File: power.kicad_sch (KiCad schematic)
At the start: 4 parts

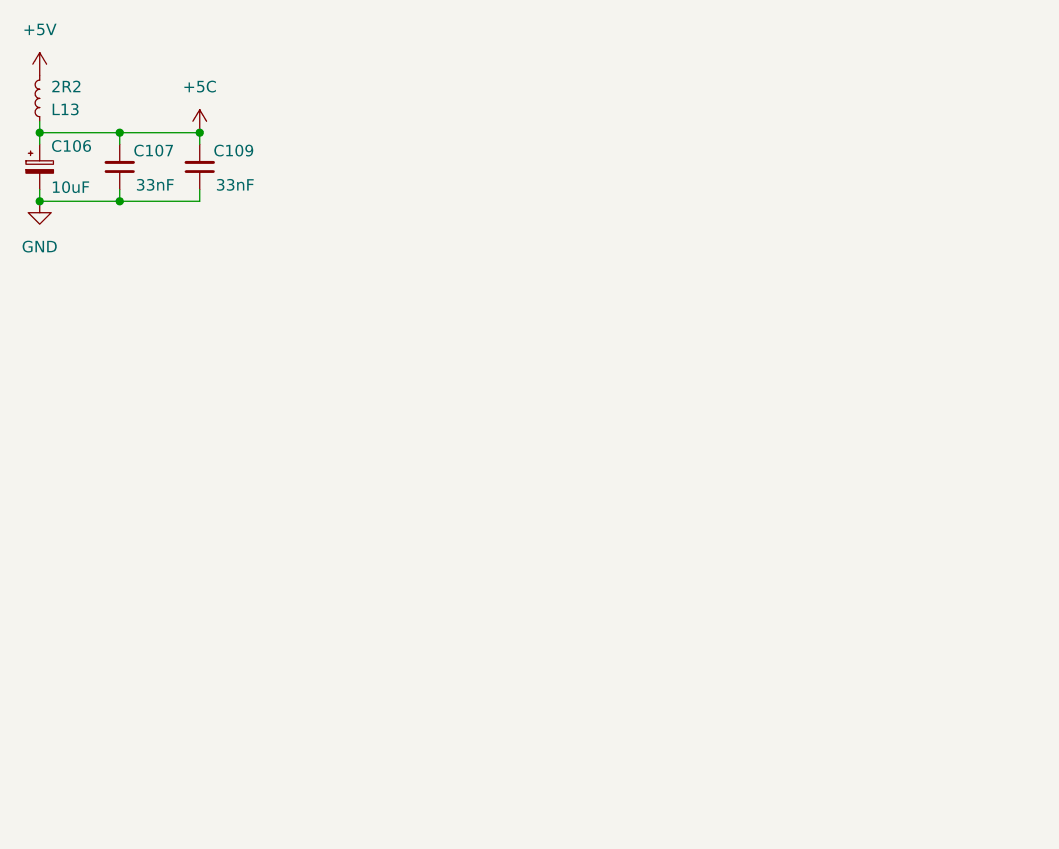
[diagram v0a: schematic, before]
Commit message: add cheeky mean well power swap
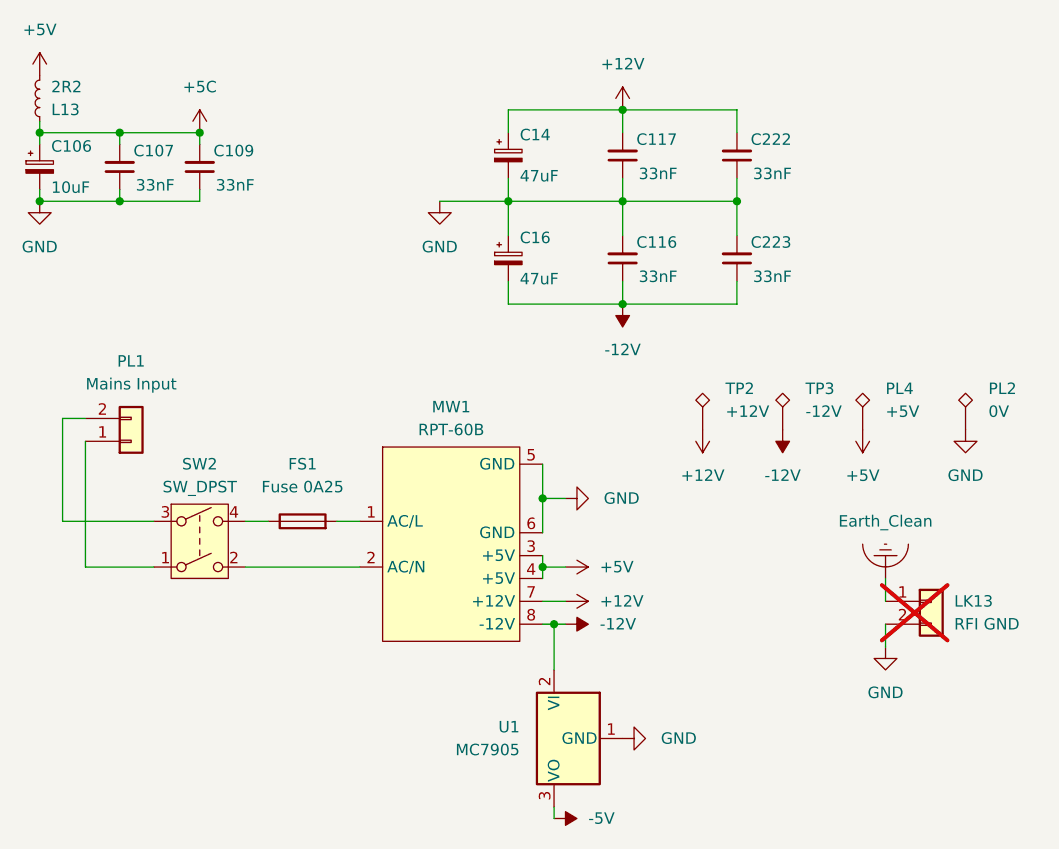
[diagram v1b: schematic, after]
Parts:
- added C116, C117, C222, C223: 33nF, Capacitor_SMD:C_0805_2012Metric, symbol Device:C_Small
- added C14, C16: 47uF, Capacitor_THT:CP_Radial_D8.0mm_P5.00mm, symbol Device:C_Polarized_Small
- added FS1: Fuse 0A25, Fuse:Fuseholder_Clip-5x20mm_Bel_FC-203-22_Lateral_P17.80x5.00mm_D1.17mm_Horizontal, symbol Device:Fuse
- added LK13: RFI GND, Connector_PinHeader_2.54mm:PinHeader_1x02_P2.54mm_Vertical, symbol Connector_Generic:Conn_01x02
- added MW1: RPT-60B, Acorn:RPT-60, symbol Acorn:RPT-60B
- added PL1: Mains Input, Connector_Molex:Molex_KK-396_A-41792-0002_1x02_P3.96mm_Horizontal, symbol Connector_Generic:Conn_01x02
- added PL2: 0V, Acorn:Molex_19708-4003, symbol Connector:TestPoint_Alt
- added PL4: +5V, Acorn:Molex_19708-4003, symbol Connector:TestPoint_Alt
- added SW2: SW_DPST, Button_Switch_THT:SW_Push_2P1T_Toggle_CK_PVA1xxH1xxxxxxV2, symbol Switch:SW_DPST
- added TP2: +12V, Acorn:Molex_19708-4003, symbol Connector:TestPoint_Alt
- added TP3: -12V, Acorn:Molex_19708-4003, symbol Connector:TestPoint_Alt
- added U1: MC7905, Package_TO_SOT_THT:TO-220-3_Horizontal_TabDown, symbol Regulator_Linear:MC7905
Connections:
- net +5V: now also MW1.3 (+5V), MW1.4 (+5V), PL4.1
- net GND: now also C116.2, C117.1, C14.2, C16.1, C222.1, C223.2, LK13.2 (Pin_2), MW1.5 (GND), MW1.6 (GND), PL2.1, U1.1 (GND)
- new net: FS1.1, SW2.4
- new net: FS1.2, MW1.1 (AC/L)
- new net: MW1.2 (AC/N), SW2.2
- new net: PL1.1 (Pin_1), SW2.1
- new net: PL1.2 (Pin_2), SW2.3
- new net +12V: C117.2, C14.1, C222.2, MW1.7 (+12V), TP2.1
- new net -12V: C116.1, C16.2, C223.1, MW1.8 (-12V), TP3.1, U1.2 (VI)
- new net -5V: U1.3 (VO)
- new net Earth_Clean: LK13.1 (Pin_1)

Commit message: fix port reference locations and lock components
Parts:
- C106: footprint Capacitor_THT:CP_Radial_D8.0mm_P5.00mm -> Capacitor_THT:CP_Radial_Tantal_D9.0mm_P5.00mm
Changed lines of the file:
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@@
 			)
 		)
-		(property "Footprint" "Capacitor_THT:CP_Radial_D8.0mm_P5.00mm"
+		(property "Footprint" "Capacitor_THT:CP_Radial_Tantal_D9.0mm_P5.00mm"
 			(at 30.48 40.64 0)
 			(effects

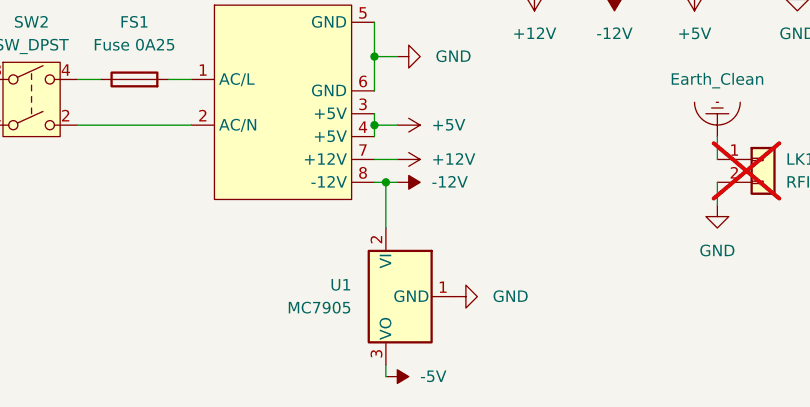
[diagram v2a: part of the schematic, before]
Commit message: remove completely unnecessary -5V rail
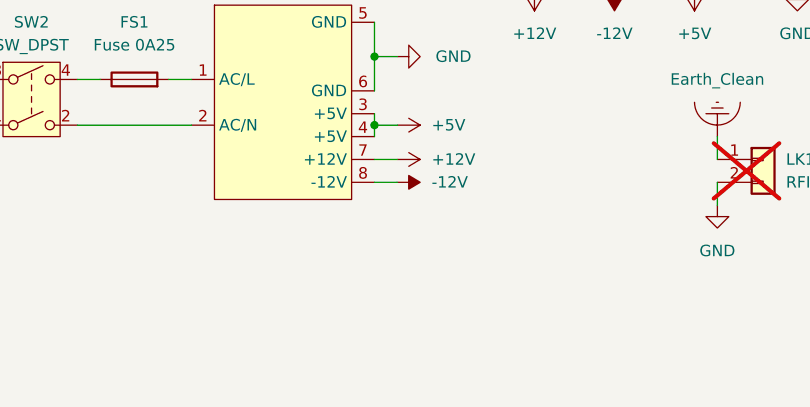
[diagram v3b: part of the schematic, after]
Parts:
- removed U1: MC7905, Package_TO_SOT_THT:TO-220-3_Horizontal_TabDown, symbol Regulator_Linear:MC7905
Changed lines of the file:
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@@
-	)
-	(junction
-		(at 87.63 91.44)
-		(diameter 0)
-		(color 0 0 0 0)
 	)
 	(junction
@@
 	(wire
 		(pts
-			(xy 87.63 96.52) (xy 87.63 91.44)
-		)
-		(stroke
-			(width 0)
-			(type default)
-		)
-	)
-	(wire
-		(pts
 			(xy 53.34 85.09) (xy 66.04 85.09)
 		)
@@
 	(wire
 		(pts
-			(xy 88.9 91.44) (xy 87.63 91.44)
-		)
-		(stroke
-			(width 0)
-			(type default)
-		)
-	)
-	(wire
-		(pts
 			(xy 95.25 41.91) (xy 95.25 44.45)
 		)
@@
 	(wire
 		(pts
-			(xy 87.63 113.03) (xy 87.63 111.76)
-		)
-		(stroke
-			(width 0)
-			(type default)
-		)
-	)
-	(wire
-		(pts
-			(xy 87.63 91.44) (xy 86.36 91.44)
+			(xy 86.36 91.44) (xy 88.9 91.44)
 		)
 		(stroke
@@
 				(path "/999882f3-94f8-4a89-9093-27a47d0cb289/5e8722fb-7afe-44d4-8a36-2936df1b76c5"
 					(reference "C222")
-					(unit 1)
-				)
-			)
-		)
-	)
-	(symbol
-		(lib_id "Regulator_Linear:MC7905")
-		(at 87.63 104.14 270)
-		(unit 1)
-		(exclude_from_sim no)
-		(in_bom yes)
-		(on_board yes)
-		(dnp no)
-		(fields_autoplaced yes)
-		(property "Reference" "U1"
-			(at 83.82 102.8699 90)
-			(effects
-				(font
-					(size 1.27 1.27)
-				)
-				(justify right)
-			)
-		)
-		(property "Value" "MC7905"
-			(at 83.82 105.4099 90)
-			(effects
-				(font
-					(size 1.27 1.27)
-				)
-				(justify right)
-			)
-		)
-		(property "Footprint" "Package_TO_SOT_THT:TO-220-3_Horizontal_TabDown"
-			(at 82.55 104.14 0)
-			(effects
-				(font
-					(size 1.27 1.27)
-					(italic yes)
-				)
-				(hide yes)
-			)
-		)
-		(property "Datasheet" "http://www.onsemi.com/pub/Collateral/MC7900-D.PDF"
-			(at 87.63 104.14 0)
-			(effects
-				(font
-					(size 1.27 1.27)
-				)
-				(hide yes)
-			)
-		)
-		(property "Description" "Negative 1A 35V Linear Regulator, Fixed Output -5V, TO-220/TO-263"
-			(at 87.63 104.14 0)
-			(effects
-				(font
-					(size 1.27 1.27)
-				)
-				(hide yes)
-			)
-		)
-		(pin "1"
-		)
-		(pin "2"
-		)
-		(pin "3"
-		)
-		(instances
-			(project ""
-				(path "/999882f3-94f8-4a89-9093-27a47d0cb289/5e8722fb-7afe-44d4-8a36-2936df1b76c5"
-					(reference "U1")
 					(unit 1)
 				)
@@
 	)
 	(symbol
-		(lib_id "power:GND")
-		(at 95.25 104.14 90)
-		(unit 1)
-		(exclude_from_sim no)
-		(in_bom yes)
-		(on_board yes)
-		(dnp no)
-		(fields_autoplaced yes)
-		(property "Reference" "#PWR0195"
-			(at 101.6 104.14 0)
-			(effects
-				(font
-					(size 1.27 1.27)
-				)
-				(hide yes)
-			)
-		)
-		(property "Value" "GND"
-			(at 99.4933 104.1399 90)
-			(effects
-				(font
-					(size 1.27 1.27)
-				)
-				(justify right)
-			)
-		)
-		(property "Footprint" ""
-			(at 95.25 104.14 0)
-			(effects
-				(font
-					(size 1.27 1.27)
-				)
-				(hide yes)
-			)
-		)
-		(property "Datasheet" ""
-			(at 95.25 104.14 0)
-			(effects
-				(font
-					(size 1.27 1.27)
-				)
-				(hide yes)
-			)
-		)
-		(property "Description" "Power symbol creates a global label with name \"GND\" , ground"
-			(at 95.25 104.14 0)
-			(effects
-				(font
-					(size 1.27 1.27)
-				)
-				(hide yes)
-			)
-		)
-		(pin "1"
-		)
-		(instances
-			(project "Acorn-A3010"
-				(path "/999882f3-94f8-4a89-9093-27a47d0cb289/5e8722fb-7afe-44d4-8a36-2936df1b76c5"
-					(reference "#PWR0195")
-					(unit 1)
-				)
-			)
-		)
-	)
-	(symbol
 		(lib_id "power:-12V")
 		(at 95.25 55.88 180)
@@
 					(unit 1)
 				)
-			)
-		)
-	)
-	(symbol
-		(lib_id "power:-5V")
-		(at 87.63 113.03 270)
-		(unit 1)
-		(exclude_from_sim no)
-		(in_bom yes)
-		(on_board yes)
-		(dnp no)
-		(fields_autoplaced yes)
-		(property "Reference" "#PWR0196"
-			(at 83.82 113.03 0)
-			(effects
-				(font
-					(size 1.27 1.27)
-				)
-				(hide yes)
-			)
-		)
-		(property "Value" "-5V"
-			(at 91.44 113.0299 90)
-			(effects
-				(font
-					(size 1.27 1.27)
-				)
-				(justify left)
-			)
-		)
-		(property "Footprint" ""
-			(at 87.63 113.03 0)
-			(effects
-				(font
-					(size 1.27 1.27)
-				)
-				(hide yes)
-			)
-		)
-		(property "Datasheet" ""
-			(at 87.63 113.03 0)
-			(effects
-				(font
-					(size 1.27 1.27)
-				)
-				(hide yes)
-			)
-		)
-		(property "Description" "Power symbol creates a global label with name \"-5V\""
-			(at 87.63 113.03 0)
-			(effects
-				(font
-					(size 1.27 1.27)
-				)
-				(hide yes)
-			)
-		)
-		(pin "1"
-		)
-		(instances
-			(project ""
-				(path "/999882f3-94f8-4a89-9093-27a47d0cb289/5e8722fb-7afe-44d4-8a36-2936df1b76c5"
-					(reference "#PWR0196")
-					(unit 1)
-				)

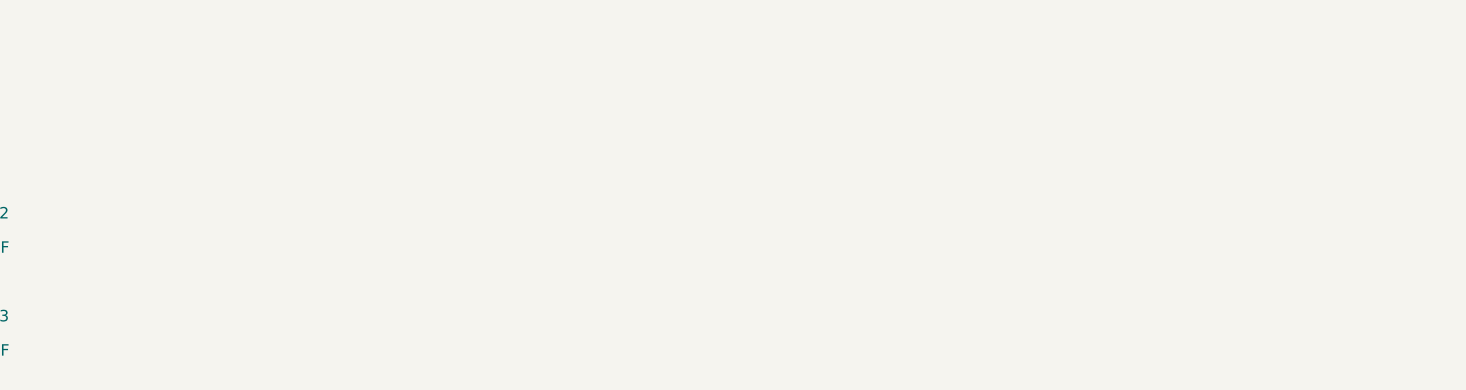
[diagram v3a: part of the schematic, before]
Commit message: data path routing
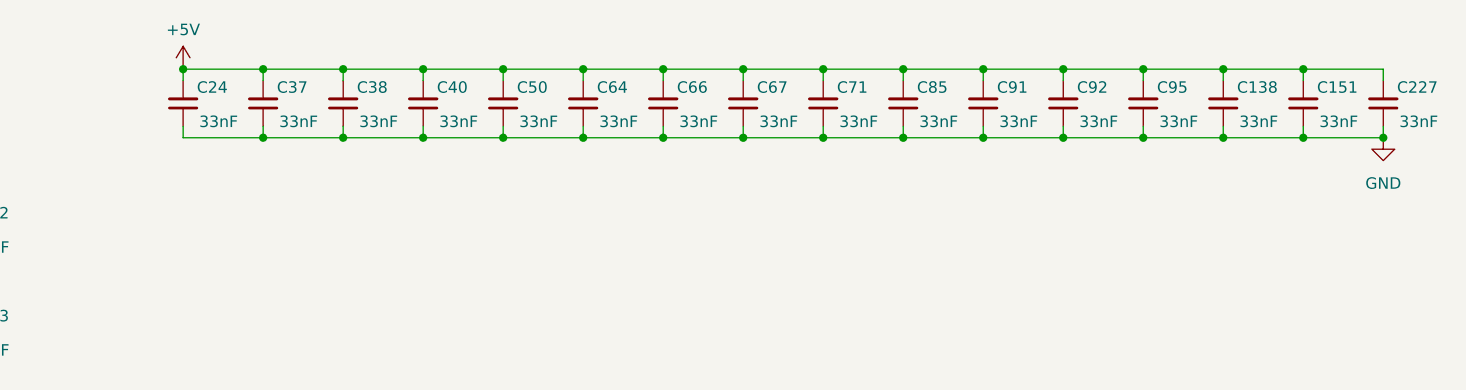
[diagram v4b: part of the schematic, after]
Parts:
- added C138, C151, C227, C24, C37, C38, C40, C50, C64, C66, C67, C71, C85, C91, C92, C95: 33nF, Capacitor_SMD:C_0805_2012Metric, symbol Device:C_Small
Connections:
- net +5V: now also C138.2, C151.2, C227.2, C24.2, C37.2, C38.2, C40.2, C50.2, C64.2, C66.2, C67.2, C71.2, C85.2, C91.2, C92.2, C95.2
- net GND: now also C138.1, C151.1, C227.1, C24.1, C37.1, C38.1, C40.1, C50.1, C64.1, C66.1, C67.1, C71.1, C85.1, C91.1, C92.1, C95.1

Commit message: more routing
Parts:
- added C161: 47uF, Capacitor_THT:CP_Radial_D8.0mm_P5.00mm, symbol Device:C_Polarized_Small
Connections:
- net +5V: now also C161.1
- net GND: now also C161.2
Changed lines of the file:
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@@
+	)
+	(symbol
+		(lib_id "Device:C_Polarized_Small")
+		(at 133.35 39.37 0)
+		(unit 1)
+		(exclude_from_sim no)
+		(in_bom yes)
+		(on_board yes)
+		(dnp no)
+		(property "Reference" "C161"
+			(at 134.62 37.084 0)
+			(effects
+				(font
+					(size 1.27 1.27)
+				)
+				(justify left)
+			)
+		)
+		(property "Value" "47uF"
+			(at 134.62 41.656 0)
+			(effects
+				(font
+					(size 1.27 1.27)
+				)
+				(justify left)
+			)
+		)
+		(property "Footprint" "Capacitor_THT:CP_Radial_D8.0mm_P5.00mm"
+			(at 133.35 39.37 0)
+			(effects
+				(font
+					(size 1.27 1.27)
+				)
+				(hide yes)
+			)
+		)
+		(property "Datasheet" "~"
+			(at 133.35 39.37 0)
+			(effects
+				(font
+					(size 1.27 1.27)
+				)
+				(hide yes)
+			)
+		)
+		(property "Description" "Polarized capacitor, small symbol"
+			(at 133.35 39.37 0)
+			(effects
+				(font
+					(size 1.27 1.27)
+				)
+				(hide yes)
+			)
+		)
+		(pin "2"
+		)
+		(pin "1"
+		)
+		(instances
+			(project "Acorn-A3010"
+				(path "/999882f3-94f8-4a89-9093-27a47d0cb289/5e8722fb-7afe-44d4-8a36-2936df1b76c5"
+					(reference "C161")
+					(unit 1)
+				)
+			)
+		)
 	)
 	(symbol
@@
 	)
 	(symbol
+		(lib_id "power:GND")
+		(at 133.35 41.91 0)
+		(unit 1)
+		(exclude_from_sim no)
+		(in_bom yes)
+		(on_board yes)
+		(dnp no)
+		(fields_autoplaced yes)
+		(property "Reference" "#PWR0282"
+			(at 133.35 48.26 0)
+			(effects
+				(font
+					(size 1.27 1.27)
+				)
+				(hide yes)
+			)
+		)
+		(property "Value" "GND"
+			(at 133.35 46.99 0)
+			(effects
+				(font
+					(size 1.27 1.27)
+				)
+			)
+		)
+		(property "Footprint" ""
+			(at 133.35 41.91 0)
+			(effects
+				(font
+					(size 1.27 1.27)
+				)
+				(hide yes)
+			)
+		)
+		(property "Datasheet" ""
+			(at 133.35 41.91 0)
+			(effects
+				(font
+					(size 1.27 1.27)
+				)
+				(hide yes)
+			)
+		)
+		(property "Description" "Power symbol creates a global label with name \"GND\" , ground"
+			(at 133.35 41.91 0)
+			(effects
+				(font
+					(size 1.27 1.27)
+				)
+				(hide yes)
+			)
+		)
+		(pin "1"
+		)
+		(instances
+			(project "Acorn-A3010"
+				(path "/999882f3-94f8-4a89-9093-27a47d0cb289/5e8722fb-7afe-44d4-8a36-2936df1b76c5"
+					(reference "#PWR0282")
+					(unit 1)
+				)
+			)
+		)
+	)
+	(symbol
 		(lib_id "Device:C_Small")
 		(at 48.26 40.64 180)
@@
 					(unit 1)
 				)
+			)
+		)
+	)
+	(symbol
+		(lib_id "power:+5V")
+		(at 133.35 36.83 0)
+		(unit 1)
+		(exclude_from_sim no)
+		(in_bom yes)
+		(on_board yes)
+		(dnp no)
+		(fields_autoplaced yes)
+		(property "Reference" "#PWR0281"
+			(at 133.35 40.64 0)
+			(effects
+				(font
+					(size 1.27 1.27)
+				)
+				(hide yes)
+			)
+		)
+		(property "Value" "+5V"
+			(at 133.35 32.4587 0)
+			(effects
+				(font
+					(size 1.27 1.27)
+				)
+			)
+		)
+		(property "Footprint" ""
+			(at 133.35 36.83 0)
+			(effects
+				(font
+					(size 1.27 1.27)
+				)
+				(hide yes)
+			)
+		)
+		(property "Datasheet" ""
+			(at 133.35 36.83 0)
+			(effects
+				(font
+					(size 1.27 1.27)
+				)
+				(hide yes)
+			)
+		)
+		(property "Description" "Power symbol creates a global label with name \"+5V\""
+			(at 133.35 36.83 0)
+			(effects
+				(font
+					(size 1.27 1.27)
+				)
+				(hide yes)
+			)
+		)
+		(pin "1"
+		)
+		(instances
+			(project "Acorn-A3010"
+				(path "/999882f3-94f8-4a89-9093-27a47d0cb289/5e8722fb-7afe-44d4-8a36-2936df1b76c5"
+					(reference "#PWR0281")
+					(unit 1)
+				)
